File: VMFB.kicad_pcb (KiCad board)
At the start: 2 copper layers, 141.6 x 109.9 mm, 113 parts, among them J1 Barrel_Jack_Switch, J10 Conn_01x03_Pin, J11 Conn_01x06_Pin, J12 Conn_01x06_Pin, J13 Conn_01x04_Pin, J14 Conn_01x03_Pin, J16 Conn_01x03_Pin, J2 USB_B, J3 Screw_Terminal_01x02, J4 Screw_Terminal_01x03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

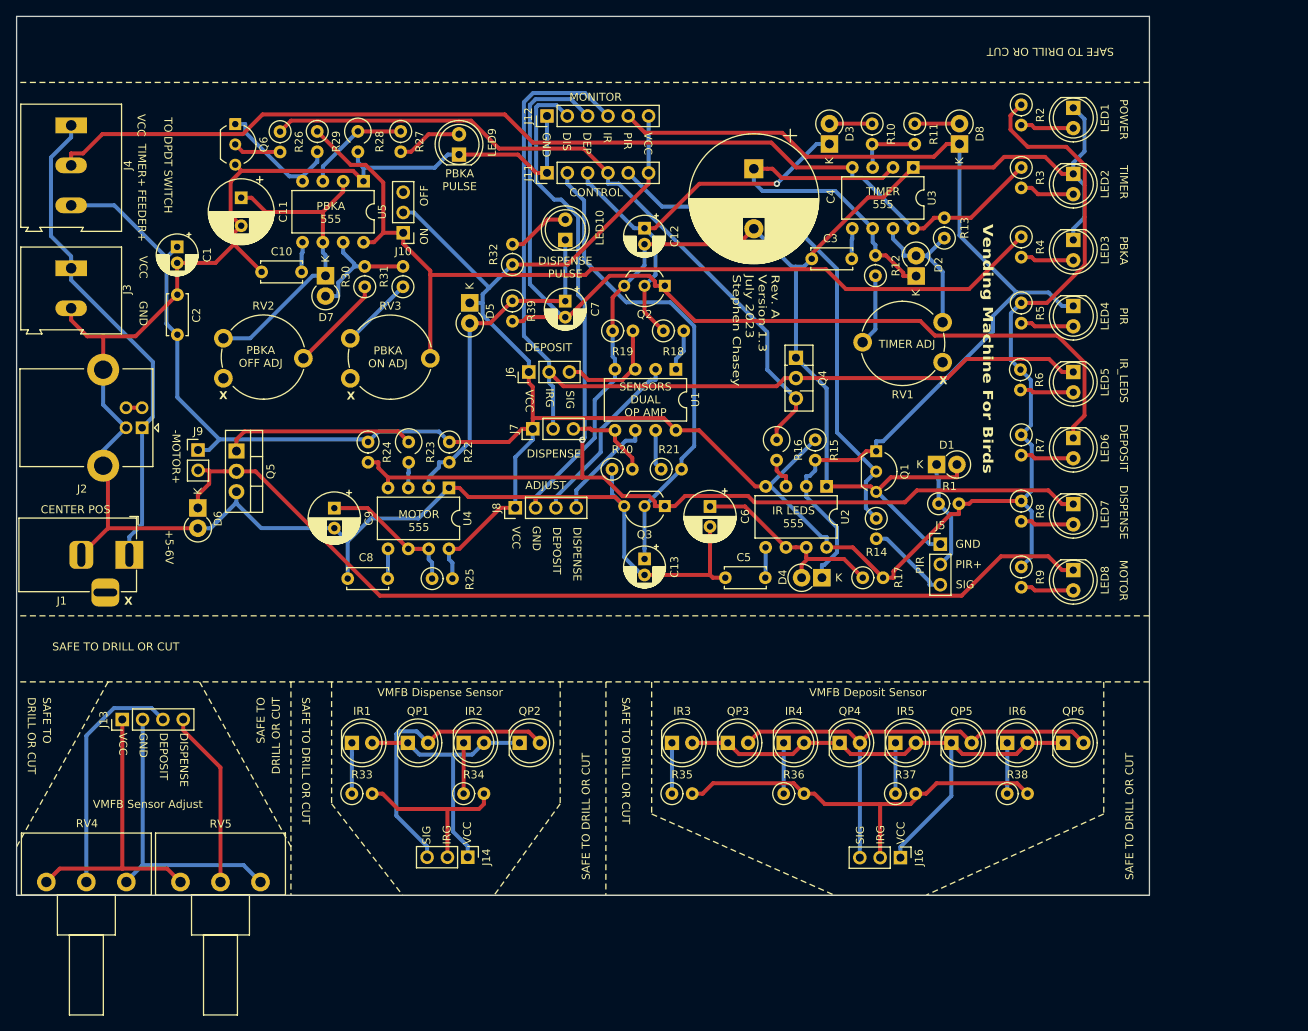
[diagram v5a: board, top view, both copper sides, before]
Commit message: added LDR-based light sensor to turn off timed dispense when the sun sets
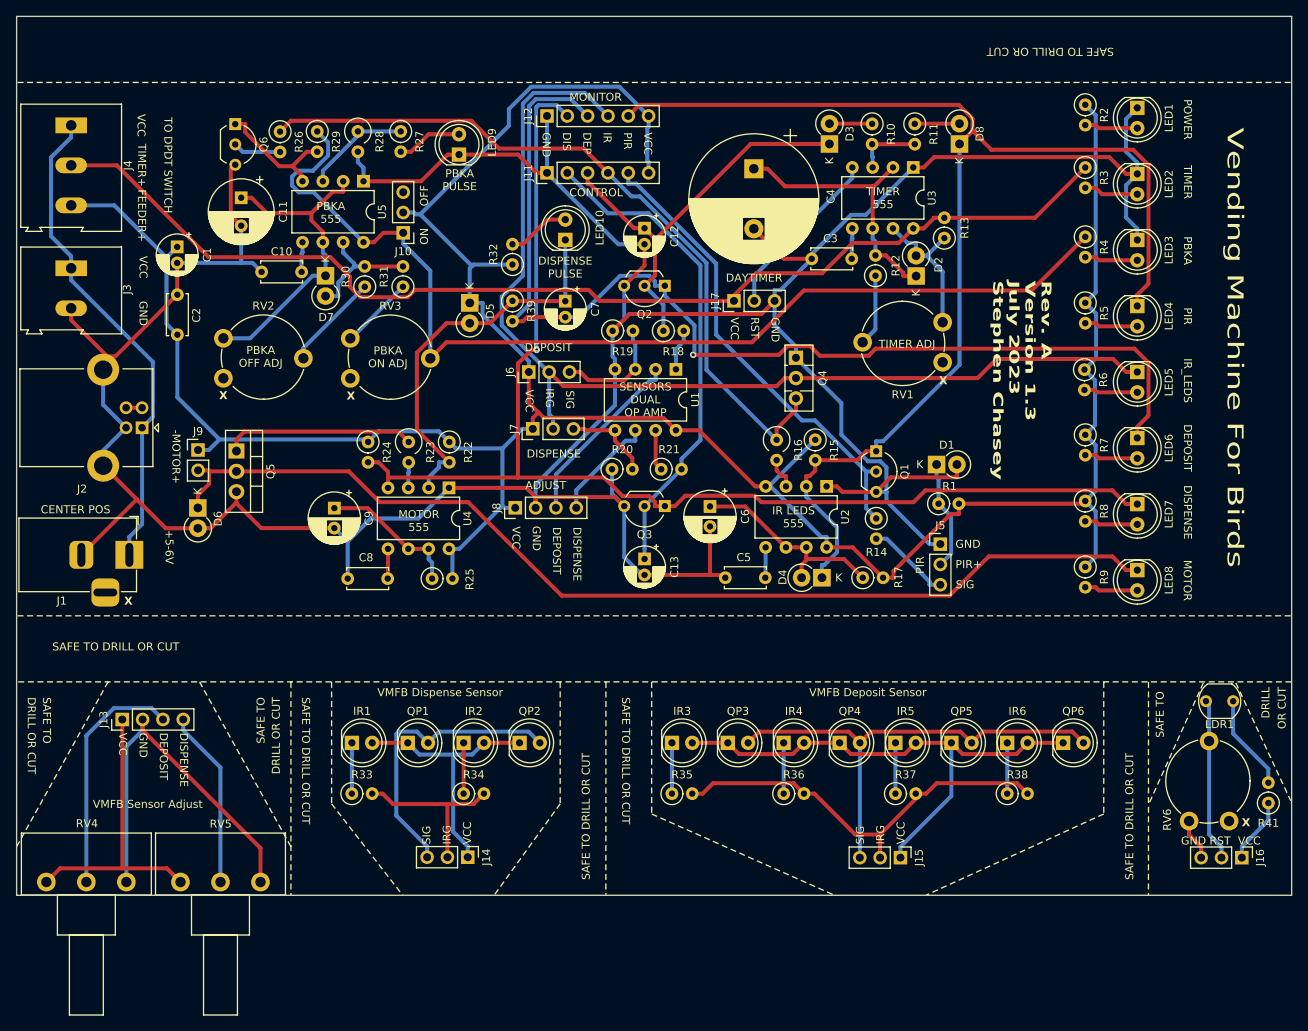
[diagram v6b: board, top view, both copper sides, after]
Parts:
- added J16: Conn_01x03_Pin, Connector_PinHeader_2.54mm:PinHeader_1x03_P2.54mm_Vertical, F.Cu at (224.3, 136.9)
- added J17: Conn_01x03_Pin, Connector_PinHeader_2.54mm:PinHeader_1x03_P2.54mm_Vertical, F.Cu at (160.8, 67.3)
- added LDR1: GL5549, OptoDevice:R_LDR_5.1x4.3mm_P3.4mm_Vertical, F.Cu at (223.2, 117.3)
- added R41: 470, Resistor_THT:R_Axial_DIN0207_L6.3mm_D2.5mm_P2.54mm_Vertical, F.Cu at (227.6, 130.1)
- added RV6: 25K, Potentiometer_THT:Potentiometer_Piher_PT-10-V10_Vertical, F.Cu at (222.7, 132.3)
- moved LED1 8.00 mm to (211.2, 43.2)
- moved LED2 8.00 mm to (211.2, 51.4)
- moved LED3 8.00 mm to (211.2, 59.7)
- moved LED4 8.00 mm to (211.2, 68.0)
- moved LED5 8.00 mm to (211.2, 76.2)
- moved LED6 8.00 mm to (211.2, 84.5)
- moved LED7 8.00 mm to (211.2, 92.7)
- moved LED8 8.00 mm to (211.2, 101.0)
- moved R2 8.00 mm to (204.7, 42.8)
- moved R3 8.00 mm to (204.7, 50.6)
- moved R4 8.00 mm to (204.7, 59.3)
- moved R5 8.00 mm to (204.7, 67.6)
- moved R6 8.00 mm to (204.6, 75.9)
- moved R7 8.00 mm to (204.7, 84.1)
- moved R8 8.00 mm to (204.7, 92.3)
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- renumbered J16 to J15
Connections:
- U3 pad 4: TIMER+ -> Net-(J17-Pin_2)
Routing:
- net PIR MON: track 127.2 -> 159.4 mm
- net GND: track 419.2 -> 444.3 mm
- net Net-(J17-Pin_2): track 0.00 -> 21.8 mm
- net Net-(J16-Pin_2): track 0.00 -> 20.4 mm
- net Net-(J10-Pin_1): track 117.6 -> 132.9 mm
- net Net-(D2-K): track 47.3 -> 34.4 mm
- net Net-(LDR1-Pad1): track 0.00 -> 12.0 mm
- net DEPOSIT MON: track 126.2 -> 137.7 mm, vias 0 -> 1
- net Net-(J13-Pin_2): track 36.8 -> 47.6 mm
- net TIMER+: track 132.1 -> 142.9 mm
- net IR GND: track 122.9 -> 133.2 mm
- net VCC: track 339.8 -> 349.7 mm
- net Net-(J16-Pin_1): track 0.00 -> 8.20 mm
- net Net-(D6-K): track 123.9 -> 131.8 mm
- net PIR CON/MON: track 65.3 -> 58.8 mm
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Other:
- board size 141.6 x 109.9 mm -> 159.4 x 109.9 mm
- board text added: "DAYTIMER"
- board text added: "DRILL"
- board text added: "OR CUT"
- board text added: "RST"

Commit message: improvements to the daytimer, and added an LED so you can see the status
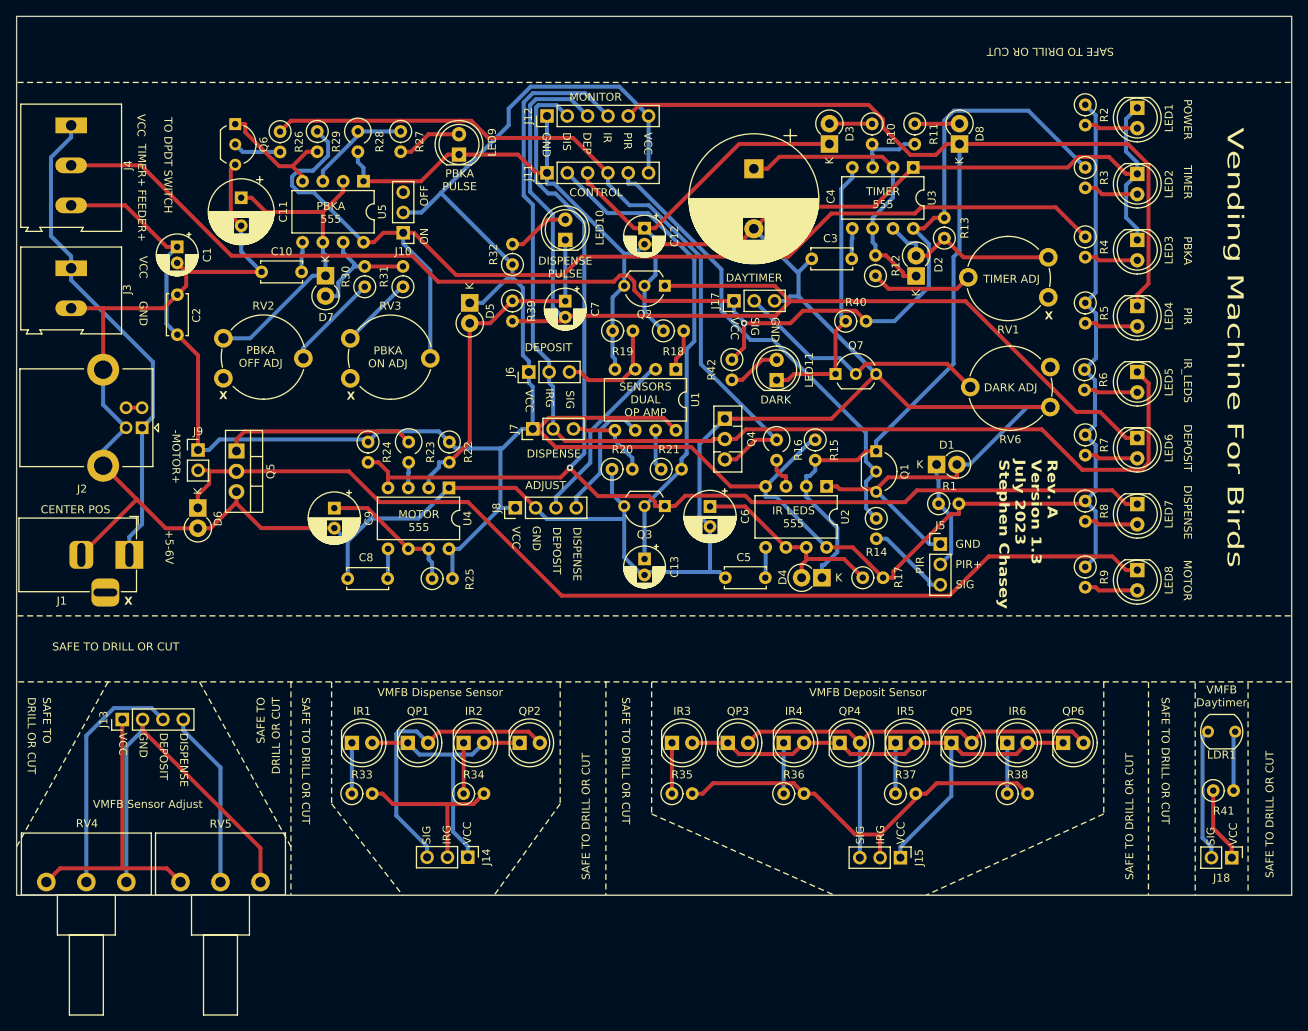
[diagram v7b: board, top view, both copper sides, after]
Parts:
- removed J16: Conn_01x03_Pin, Connector_PinHeader_2.54mm:PinHeader_1x03_P2.54mm_Vertical
- added J18: Conn_01x02_Pin, Connector_PinHeader_2.54mm:PinHeader_1x02_P2.54mm_Vertical, F.Cu at (223.0, 136.9)
- added LED11: Signal LED, LED_THT:LED_D5.0mm, F.Cu at (166.1, 77.2)
- added Q7: BC547, Package_TO_SOT_THT:TO-92_Inline_Wide, F.Cu at (173.5, 76.5)
- added R40: 10K, Resistor_THT:R_Axial_DIN0207_L6.3mm_D2.5mm_P2.54mm_Vertical, F.Cu at (174.8, 69.8)
- added R42: 10K, Resistor_THT:R_Axial_DIN0207_L6.3mm_D2.5mm_P2.54mm_Vertical, F.Cu at (160.5, 74.6)
- R12: value 100K -> 220K
- RV1: value 1M -> 2M
- RV6: value 25K -> 10K
- moved RV6 61.0 mm to (200.3, 75.6), turned to 180 degrees
- moved RV1 15.5 mm to (200.1, 61.9)
- moved Q4 11.7 mm to (159.6, 82.0)
- moved R41 7.06 mm to (220.7, 128.5), turned to 0 degrees
- moved LDR1 3.82 mm to (223.4, 121.2)
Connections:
- LDR1 pad 2: Net-(J16-Pin_2) -> Net-(J18-Pin_2)
- RV6 pad 2: Net-(J16-Pin_2) -> Net-(J17-Pin_2)
- RV6 pad 3: Net-(J16-Pin_3) -> GND
- U3 pad 4: Net-(J17-Pin_2) -> Net-(LED11-K)
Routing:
- net Net-(LED11-K): track 0.00 -> 34.8 mm
- net GND: track 444.3 -> 478.4 mm
- net TIMER+: track 142.9 -> 171.5 mm, vias 0 -> 1
- net VCC: track 349.7 -> 370.6 mm
- net Net-(J16-Pin_2): track 20.4 -> 0.00 mm
- net Net-(J18-Pin_2): track 0.00 -> 16.5 mm
- net IR GND: track 133.2 -> 144.6 mm
- net Net-(J17-Pin_2): track 21.8 -> 32.5 mm
- net Net-(LED11-A): track 0.00 -> 6.63 mm
- net Net-(J16-Pin_3): track 5.20 -> 0.00 mm
- net MOTOR TRIGGER: track 49.3 -> 44.2 mm
- net Net-(D2-A): track 18.8 -> 23.8 mm
- net Net-(LDR1-Pad1): track 12.0 -> 7.45 mm
- net Net-(J10-Pin_1): track 132.9 -> 137.2 mm
- net Net-(R12-Pad1): track 8.98 -> 12.9 mm
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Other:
- board text added: "DARK"
- board text added: "DARK ADJ"
- board text added: "VMFB Daytimer"
- board text removed: "DRILL"
- board text removed: "OR CUT"
- board text removed: "RST"

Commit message: minor adjustments to the daytimer
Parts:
- added R43: 470R, Resistor_THT:R_Axial_DIN0207_L6.3mm_D2.5mm_P2.54mm_Vertical, F.Cu at (187.2, 75.7)
- R40: value 10K -> 22K
- RV6: value 10K -> 25K
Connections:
- RV6 pad 2: Net-(J17-Pin_2) -> Net-(R43-Pad2)
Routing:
- net GND: track 478.4 -> 0.00 mm
- net VCC: track 370.6 -> 0.00 mm
- net TIMER+: track 171.5 -> 0.00 mm, vias 1 -> 0
- net PIR MON: track 157.5 -> 0.00 mm
- net MOTOR RESET: track 157.0 -> 0.00 mm, vias 1 -> 0
- net IR GND: track 144.6 -> 0.00 mm
- net DEPOSIT MON: track 139.6 -> 0.00 mm
- net Net-(J10-Pin_1): track 137.2 -> 0.00 mm
- net Net-(D6-K): track 131.8 -> 0.00 mm
- net IR CON/MON: track 95.2 -> 0.00 mm
- net Net-(IR3-A): track 66.8 -> 0.00 mm
- net Net-(J2-VBUS): track 61.2 -> 0.00 mm
- net DISPENSE CON/MON: track 60.4 -> 0.00 mm
- net Net-(J15-Pin_3): track 59.8 -> 0.00 mm
- net PIR CON/MON: track 59.3 -> 0.00 mm
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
